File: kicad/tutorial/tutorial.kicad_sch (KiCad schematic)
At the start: 1 part

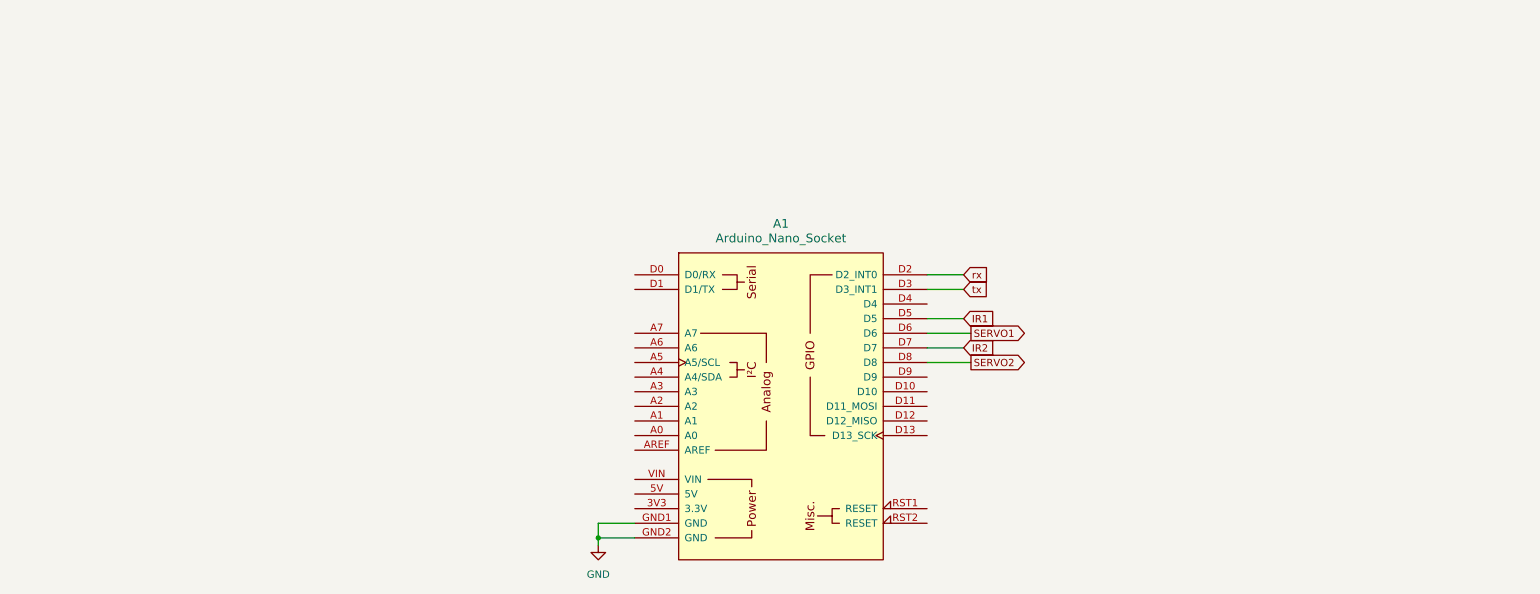
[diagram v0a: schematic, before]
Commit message: foot print error
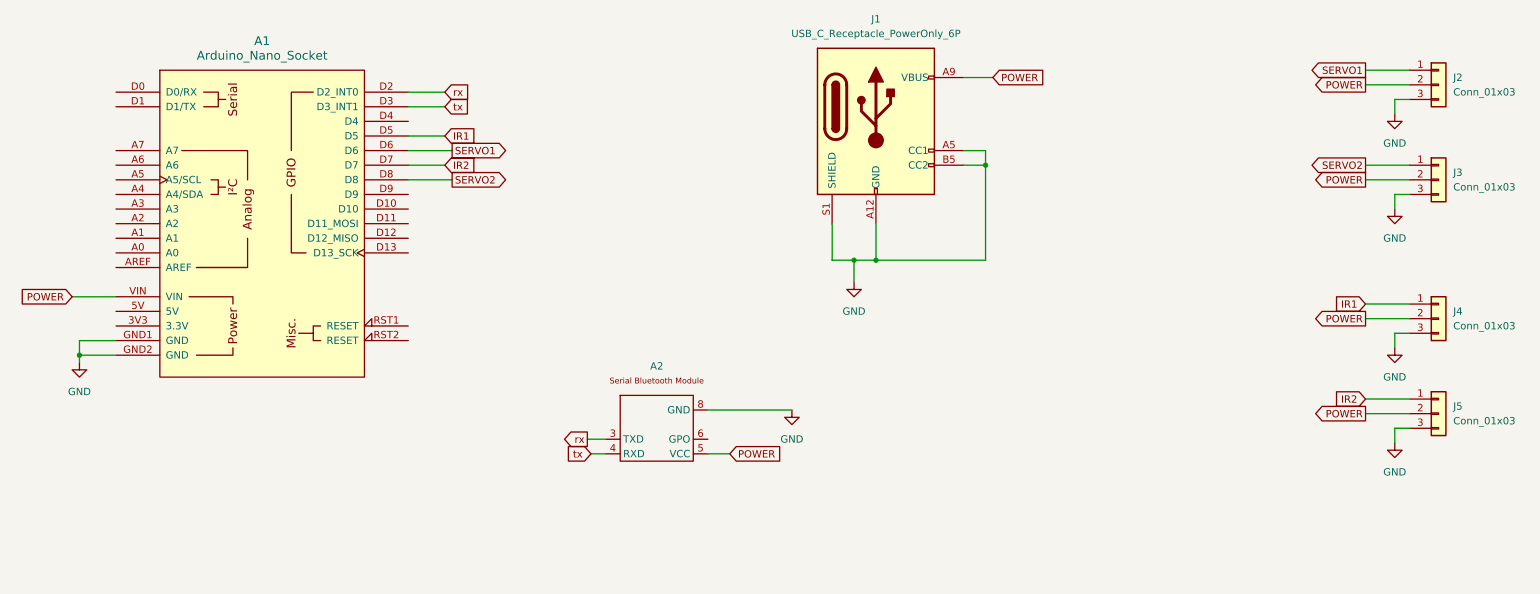
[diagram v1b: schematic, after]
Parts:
- added A2: ~, project_lib:Bluetooth_Serial, symbol project_lib:Serial_bluetooth
- added J1: USB_C_Receptacle_PowerOnly_6P, Connector_USB:USB_C_Receptacle_XKB_U262-16XN-4BVC11, symbol Connector:USB_C_Receptacle_PowerOnly_6P
- added J2, J3, J4, J5: Conn_01x03, Connector_PinHeader_2.54mm:PinHeader_1x03_P2.54mm_Vertical, symbol Connector_Generic:Conn_01x03
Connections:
- net GND: now also A2.8 (GND), J1.A12 (GND), J1.A5 (CC1), J1.B12 (GND), J1.B5 (CC2), J1.S1 (SHIELD), J2.3 (Pin_3), J3.3 (Pin_3), J4.3 (Pin_3), J5.3 (Pin_3)
- net IR1: now also J4.1 (Pin_1)
- net IR2: now also J5.1 (Pin_1)
- net SERVO1: now also J2.1 (Pin_1)
- net SERVO2: now also J3.1 (Pin_1)
- net rx: now also A2.3 (TXD)
- net tx: now also A2.4 (RXD)
- net POWER: now reaches A1.VIN
- net POWER: now also A2.5 (VCC), J1.A9 (VBUS), J1.B9 (VBUS), J2.2 (Pin_2), J3.2 (Pin_2), J4.2 (Pin_2), J5.2 (Pin_2)
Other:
- moved on the sheet: A1
